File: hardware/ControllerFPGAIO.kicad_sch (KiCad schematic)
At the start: 1 part, among them U4 XC7S25-1CSGA225C

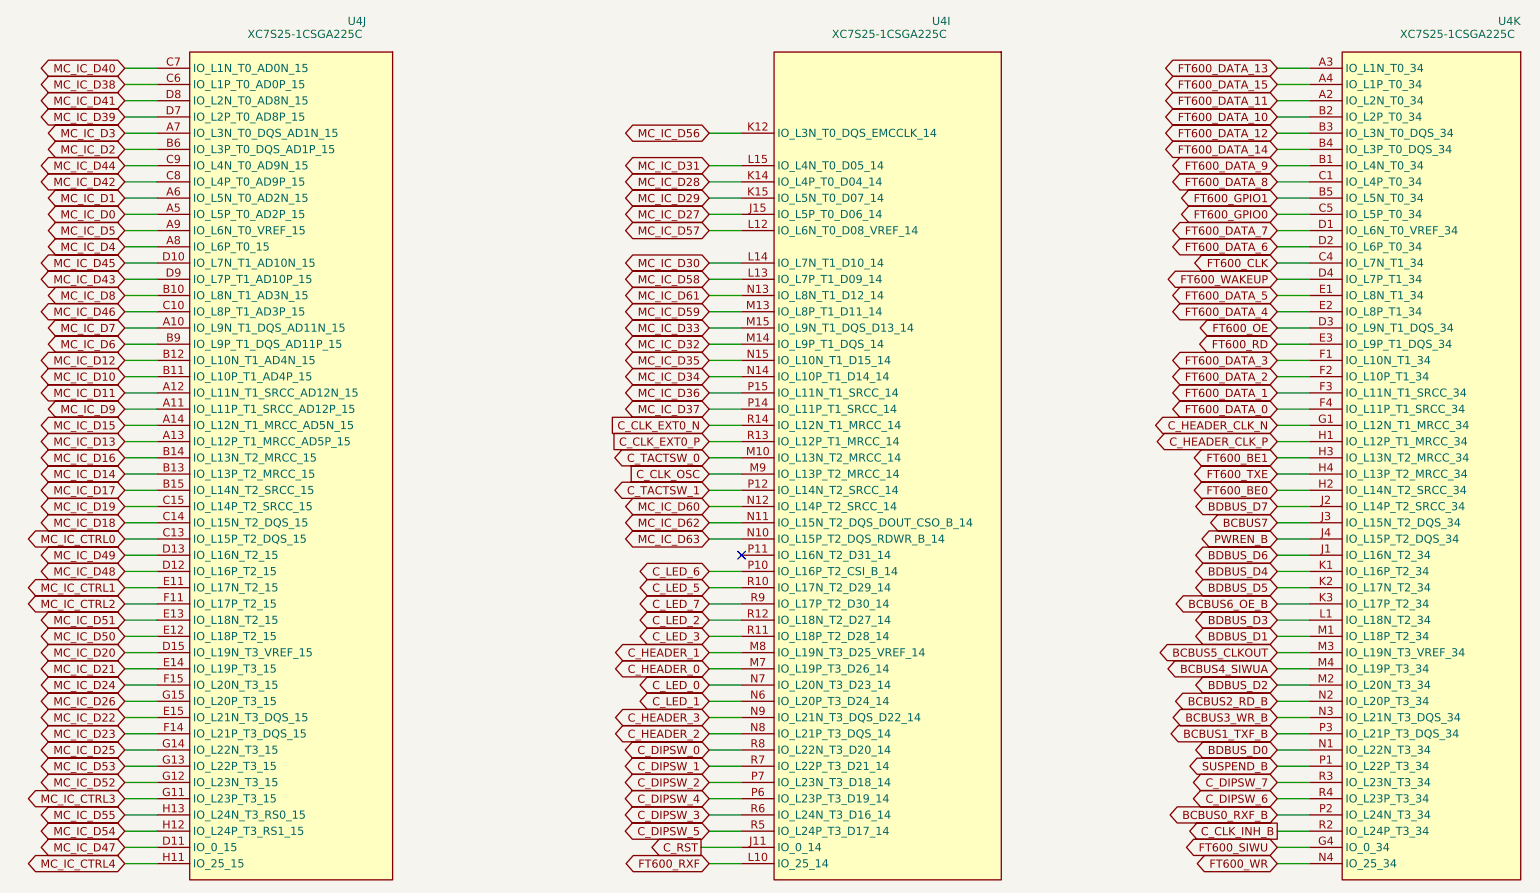
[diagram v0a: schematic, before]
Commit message: Update hardware design and include board logo
Sync the saved schematics, PCB, project settings, and referenced custom
libraries with the updated design. Include the LOGO footprint and register
it in the project footprint table. The board now contains 524 footprints.

Keep unused source libraries, autosaves, backups, analysis outputs, and
manufacturing files out of the import. Point BOM exports to the existing
ignored production directory instead of a workstation-specific location.

Validation with KiCad 9.0.1:
- Netlist export succeeds and referenced custom libraries resolve.
- DRC: 0 errors, 40 warnings, 0 unconnected items, 0 schematic mismatches.
- ERC: 27 errors and 71 warnings, identical to the source design.

The pre-existing missing JTAG 3D model (87831-1420.stp) is not supplied by
the source project and remains unresolved.
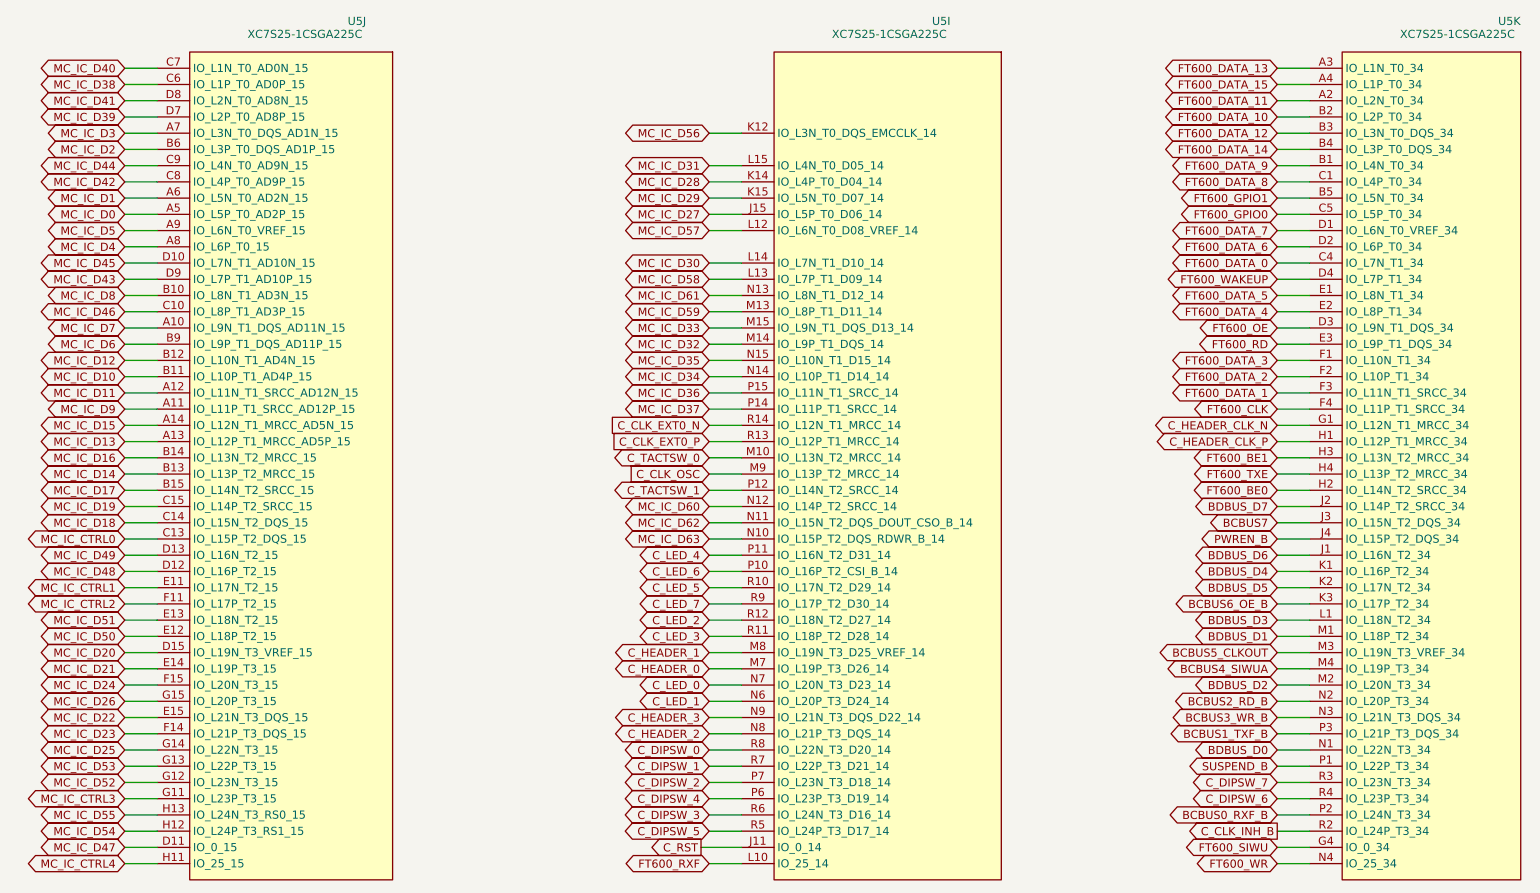
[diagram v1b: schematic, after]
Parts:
- renumbered U4 to U5
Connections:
- net FT600_CLK: now also U5.F4 (IO_L11P_T1_SRCC_34); no longer U5.C4 (IO_L7N_T1_34)
- net FT600_DATA_0: now also U5.C4 (IO_L7N_T1_34); no longer U5.F4 (IO_L11P_T1_SRCC_34)
- net C_LED_4: now reaches U5.P11 (IO_L16N_T2_D31_14)
- no-connect marks 1 -> 0
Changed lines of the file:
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@@
 	(generator_version "9.0")
 	(paper "A4")
-	(no_connect
-		(at 134.62 104.14)
-	)
 	(wire
 		(pts
@@
 	(wire
 		(pts
+			(xy 134.62 104.14) (xy 129.54 104.14)
+		)
+		(stroke
+			(width 0)
+			(type default)
+		)
+	)
+	(wire
+		(pts
 			(xy 218.44 40.64) (xy 223.52 40.64)
 		)
@@
 	(wire
 		(pts
+			(xy 218.44 81.28) (xy 223.52 81.28)
+		)
+		(stroke
+			(width 0)
+			(type default)
+		)
+	)
+	(wire
+		(pts
 			(xy 38.1 144.78) (xy 43.18 144.78)
 		)
@@
 	(wire
 		(pts
-			(xy 218.44 81.28) (xy 223.52 81.28)
-		)
-		(stroke
-			(width 0)
-			(type default)
-		)
-	)
-	(wire
-		(pts
 			(xy 218.44 55.88) (xy 223.52 55.88)
 		)
@@
 		)
 	)
+	(global_label "FT600_DATA_0"
+		(shape bidirectional)
+		(at 218.44 58.42 180)
+		(fields_autoplaced yes)
+		(effects
+			(font
+				(size 1.27 1.27)
+			)
+			(justify right)
+		)
+		(property "Intersheetrefs" "${INTERSHEET_REFS}"
+			(at 203.216 58.42 0)
+			(effects
+				(font
+					(size 1.27 1.27)
+				)
+				(justify right)
+				(hide yes)
+			)
+		)
+	)
 	(global_label "MC_IC_D19"
 		(shape bidirectional)
@@
 		)
 	)
-	(global_label "FT600_CLK"
-		(shape bidirectional)
-		(at 218.44 58.42 180)
-		(fields_autoplaced yes)
-		(effects
-			(font
-				(size 1.27 1.27)
-			)
-			(justify right)
-		)
-		(property "Intersheetrefs" "${INTERSHEET_REFS}"
-			(at 203.216 58.42 0)
-			(effects
-				(font
-					(size 1.27 1.27)
-				)
-				(justify right)
-				(hide yes)
-			)
-		)
-	)
 	(global_label "FT600_DATA_8"
 		(shape bidirectional)
@@
 		)
 	)
-	(global_label "FT600_DATA_0"
-		(shape bidirectional)
-		(at 218.44 81.28 180)
-		(fields_autoplaced yes)
-		(effects
-			(font
-				(size 1.27 1.27)
-			)
-			(justify right)
-		)
-		(property "Intersheetrefs" "${INTERSHEET_REFS}"
-			(at 203.216 81.28 0)
-			(effects
-				(font
-					(size 1.27 1.27)
-				)
-				(justify right)
-				(hide yes)
-			)
-		)
-	)
 	(global_label "C_DIPSW_4"
 		(shape bidirectional)
@@
 		)
 	)
+	(global_label "FT600_CLK"
+		(shape bidirectional)
+		(at 218.44 81.28 180)
+		(fields_autoplaced yes)
+		(effects
+			(font
+				(size 1.27 1.27)
+			)
+			(justify right)
+		)
+		(property "Intersheetrefs" "${INTERSHEET_REFS}"
+			(at 203.216 81.28 0)
+			(effects
+				(font
+					(size 1.27 1.27)
+				)
+				(justify right)
+				(hide yes)
+			)
+		)
+	)
 	(global_label "MC_IC_CTRL0"
 		(shape bidirectional)
@@
 		)
 	)
+	(global_label "C_LED_4"
+		(shape bidirectional)
+		(at 129.54 104.14 180)
+		(fields_autoplaced yes)
+		(effects
+			(font
+				(size 1.27 1.27)
+			)
+			(justify right)
+		)
+		(property "Intersheetrefs" "${INTERSHEET_REFS}"
+			(at 114.316 104.14 0)
+			(effects
+				(font
+					(size 1.27 1.27)
+				)
+				(justify right)
+				(hide yes)
+			)
+		)
+	)
 	(global_label "C_CLK_EXT0_P"
 		(shape input)
@@
 		(on_board yes)
 		(dnp no)
-		(property "Reference" "U4"
+		(property "Reference" "U5"
 			(at 74.422 20.574 0)
 			(effects
@@
 			(project "shamiko"
 				(path "/3bdb682e-16f1-4662-9b00-b0c9070eb240/a0ad8467-7f2d-4c5a-a9f6-c00590d46d0c"
-					(reference "U4")
+					(reference "U5")
 					(unit 10)
 				)
@@
 		(on_board yes)
 		(dnp no)
-		(property "Reference" "U4"
+		(property "Reference" "U5"
 			(at 254.762 20.574 0)
 			(effects
@@
 			(project ""
 				(path "/3bdb682e-16f1-4662-9b00-b0c9070eb240/a0ad8467-7f2d-4c5a-a9f6-c00590d46d0c"
-					(reference "U4")
+					(reference "U5")
 					(unit 11)
 				)
@@
 		(on_board yes)
 		(dnp no)
-		(property "Reference" "U4"
+		(property "Reference" "U5"
 			(at 165.862 20.574 0)
 			(effects
@@
 			(project "shamiko"
 				(path "/3bdb682e-16f1-4662-9b00-b0c9070eb240/a0ad8467-7f2d-4c5a-a9f6-c00590d46d0c"
-					(reference "U4")
+					(reference "U5")
 					(unit 9)
 				)
